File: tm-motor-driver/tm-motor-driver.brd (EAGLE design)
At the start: 68.6 x 19.1 mm, 19 parts

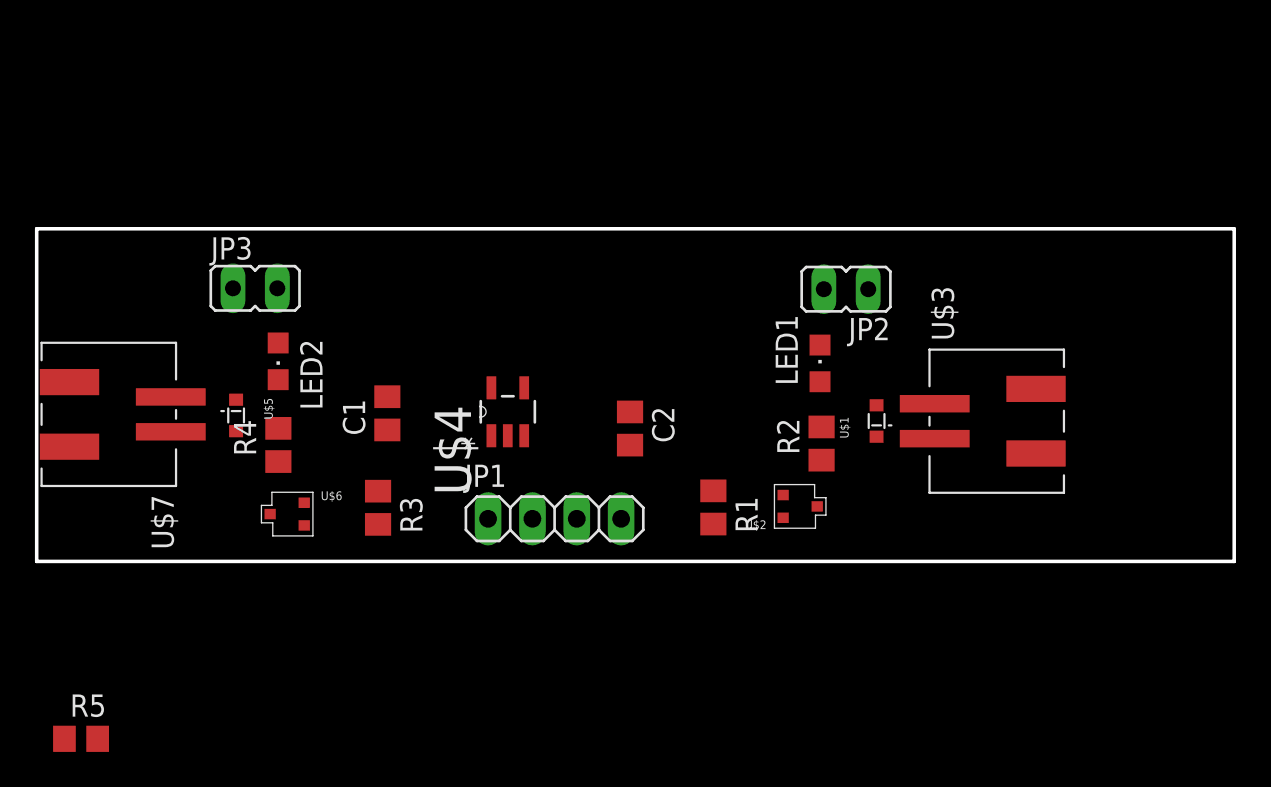
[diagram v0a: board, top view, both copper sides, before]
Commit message: Remove jumpers, rearrange LED and series resistor for easier layout
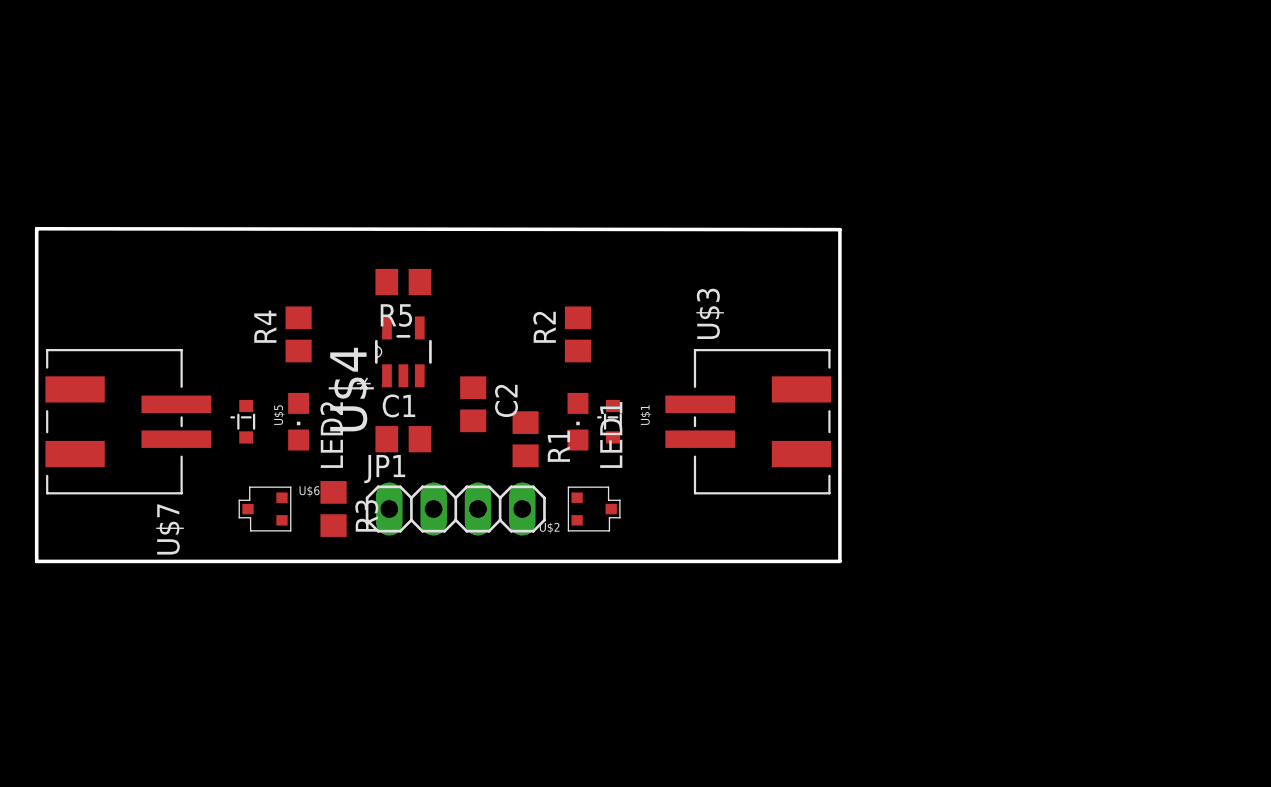
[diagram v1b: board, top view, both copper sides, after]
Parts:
- removed JP2, JP3: (no value), jumper:JP1
- moved R5 32.0 mm to (21.0, 16.0), turned to 180 degrees
- moved R2 15.3 mm to (31.0, 13.0)
- moved U$1 15.1 mm to (33.0, 8.00), turned to 180 degrees
- moved LED1 14.3 mm to (31.0, 8.00), turned to 180 degrees
- moved U$3 13.4 mm to (40.0, 8.00)
- moved U$2 11.8 mm to (32.0, 3.00)
- moved R1 11.4 mm to (28.0, 7.00)
- moved C2 9.09 mm to (25.0, 9.00)
- moved U$4 6.89 mm to (21.0, 12.0)
- moved R4 6.44 mm to (15.0, 13.0)
- moved JP1 5.69 mm to (24.0, 3.00)
- moved LED2 3.65 mm to (15.0, 8.00)
- moved R3 2.55 mm to (17.0, 3.00)
- moved C1 1.74 mm to (21.0, 7.00), turned to 0 degrees
- moved U$6 1.30 mm to (13.0, 3.00)
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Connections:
- removed net N$5: JP3.2, LED2.A
- removed net N$6: LED2.C, R4.2
- net +3V3: now also R2.2, R4.2; no longer JP2.1, JP3.1
- net N$1: now also LED2.C; no longer R4.1
- net N$2: now also LED1.C; no longer R2.1
- net N$3: now also R2.1; no longer JP2.2
- net N$4: now also LED2.A, R4.1; no longer LED1.C, R2.2
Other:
- board size 68.6 x 19.1 mm -> 46 x 19.1 mm

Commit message: Change header to JST
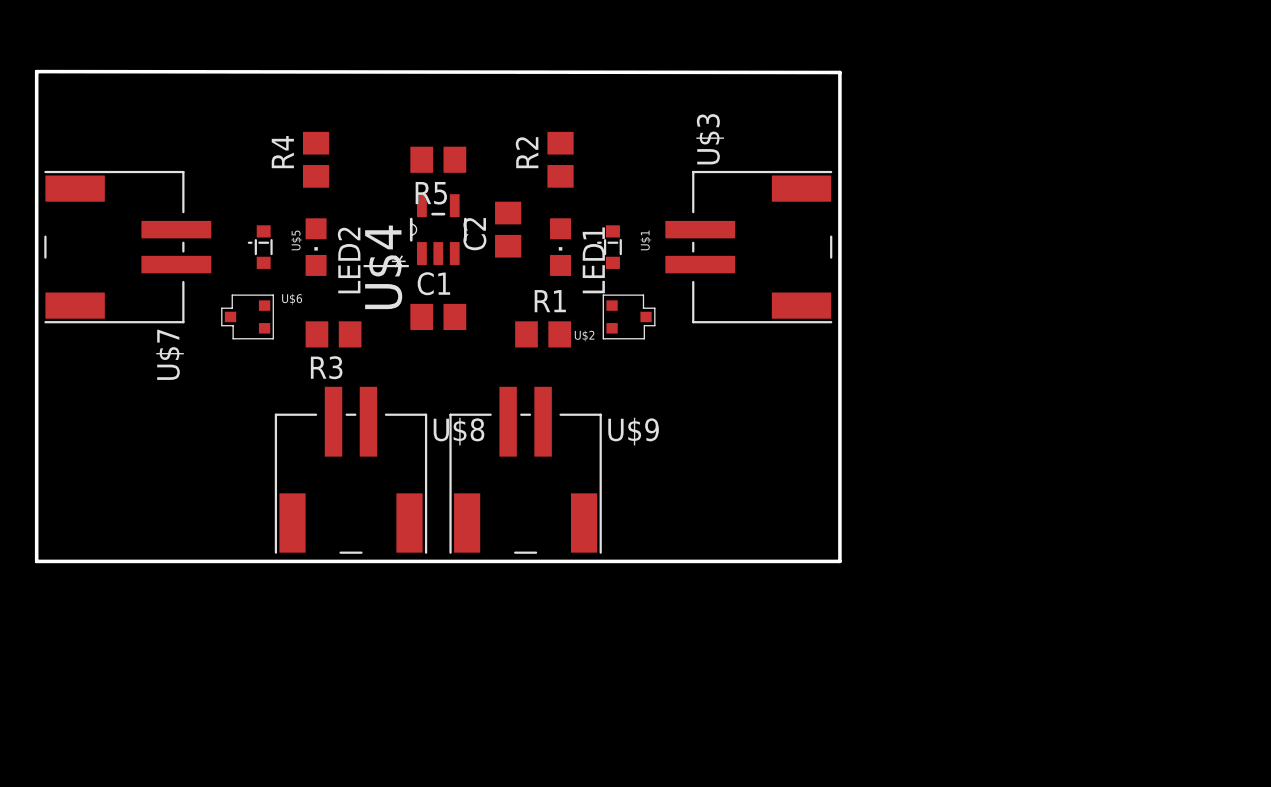
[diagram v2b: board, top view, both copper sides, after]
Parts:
- removed JP1: (no value), pinhead:1X04
- added U$8, U$9: JST-SMD-2, tactile-music:JST-SMD-2
- moved U$2 11.2 mm to (34.0, 14.0)
- moved U$6 11.0 mm to (12.0, 14.0)
- moved C2 10.2 mm to (27.0, 19.0), turned to 90 degrees
- moved LED1 10.0 mm to (30.0, 18.0)
- moved LED2 10.0 mm to (16.0, 18.0)
- moved R2 10.0 mm to (30.0, 23.0)
- moved R4 10.0 mm to (16.0, 23.0)
- moved U$5 10.0 mm to (13.0, 18.0)
- moved R3 10.0 mm to (17.0, 13.0), turned to 180 degrees
- moved U$1 10.0 mm to (33.0, 18.0)
- moved U$3 10.0 mm to (40.0, 18.0)
- moved U$7 10.0 mm to (6.00, 18.0)
- moved C1 7.28 mm to (23.0, 14.0)
- moved R5 7.28 mm to (23.0, 23.0)
- moved U$4 7.28 mm to (23.0, 19.0)
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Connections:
- net BATT_V+: now also U$8.2; no longer JP1.4
- net GND: now also U$8.1; no longer JP1.3
- net PWM0: now also U$9.2; no longer JP1.2
- net PWM1: now also U$9.1; no longer JP1.1
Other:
- board size 46 x 19.1 mm -> 46 x 28.1 mm

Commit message: Change MOTOR_0 JST connections to make PCB routing easier
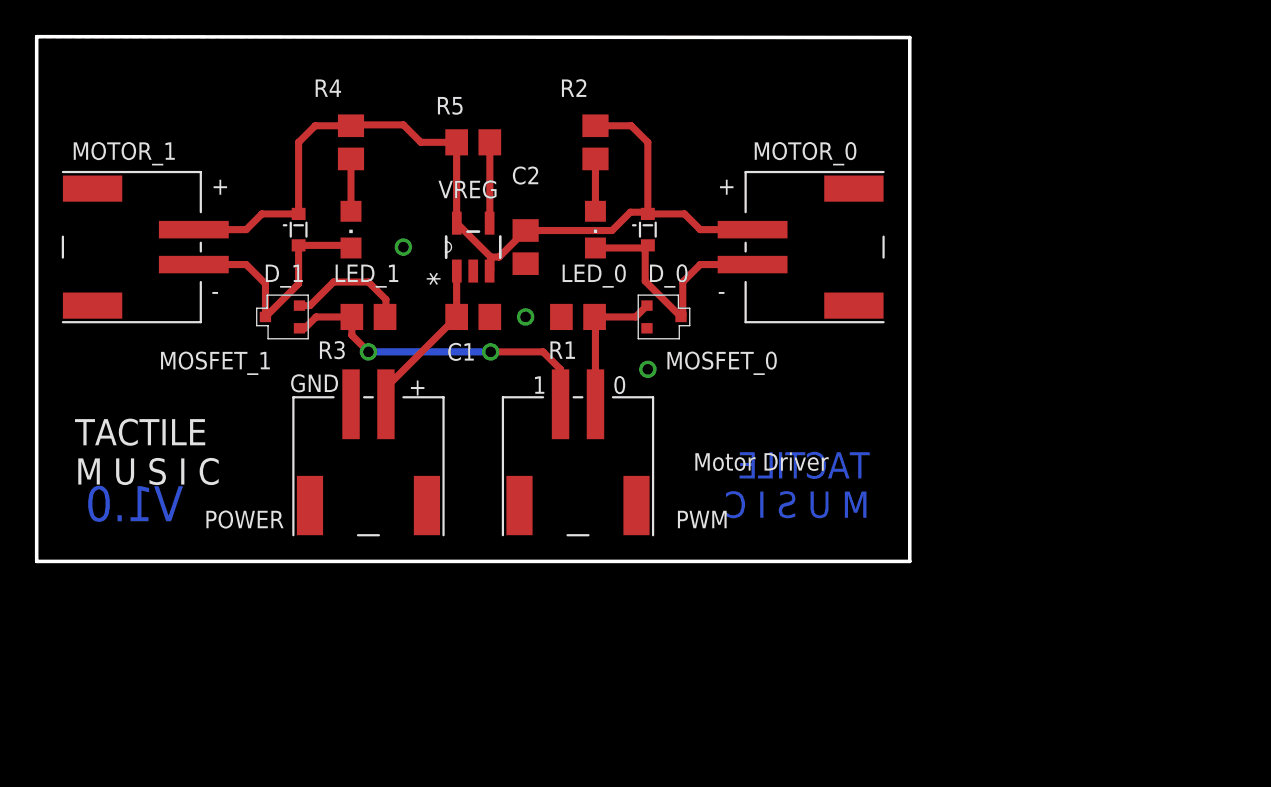
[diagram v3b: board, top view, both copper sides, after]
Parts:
- removed LED1, LED2: (no value), led:CHIPLED_0805
- removed U$1, U$5: DB2S308, tactile-music:SOD-523
- removed U$2, U$6: PMF370XN, tactile-music:SOT323(SC-70)
- removed U$3, U$7, U$8, U$9: JST-SMD-2, tactile-music:JST-SMD-2
- removed U$4: MCP1824T-3302E/OT, tactile-music:SOT95P270X145-5N
- added D_0, D_1: DB2S308, tactile-music:SOD-523
- added LED_0, LED_1: (no value), led:CHIPLED_0805
- added MOSFET_0, MOSFET_1: PMF370XN, tactile-music:SOT323(SC-70)
- added MOTOR_0, MOTOR_1, POWER, PWM: JST-SMD-2, tactile-music:JST-SMD-2
- added VREG: MCP1824T-3302E/OT, tactile-music:SOT95P270X145-5N
- moved R1 2.24 mm to (31.0, 14.0)
- moved R2 2.24 mm to (32.0, 24.0)
- moved R3 2.24 mm to (19.0, 14.0)
- moved R4 2.24 mm to (18.0, 24.0)
- moved R5 2.24 mm to (25.0, 24.0)
- moved C1 2.00 mm to (25.0, 14.0)
- moved C2 1.41 mm to (28.0, 18.0), turned to 270 degrees
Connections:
- net +3V3: now also D_0.1, D_1.1, MOTOR_0.2, MOTOR_1.1, VREG.3, VREG.5; no longer U$1.1, U$3.1, U$4.3, U$4.5, U$5.1, U$7.1
- net BATT_V+: now also POWER.2, VREG.1; no longer U$4.1, U$8.2
- net GND: now also MOSFET_0.2, MOSFET_1.2, POWER.1, VREG.2; no longer U$2.2, U$4.2, U$6.2, U$8.1
- net N$1: now also D_1.2, LED_1.C, MOSFET_1.3, MOTOR_1.2; no longer LED2.C, U$5.2, U$6.3, U$7.2
- net N$2: now also D_0.2, LED_0.C, MOSFET_0.3, MOTOR_0.1; no longer LED1.C, U$1.2, U$2.3, U$3.2
- net N$3: now also LED_0.A; no longer LED1.A
- net N$4: now also LED_1.A; no longer LED2.A
- net N$7: now also VREG.4; no longer U$4.4
- net PWM0: now also MOSFET_0.1, PWM.2; no longer U$2.1, U$9.2
- net PWM1: now also MOSFET_1.1, PWM.1; no longer U$6.1, U$9.1
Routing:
- net +3V3: track 0.00 -> 53.0 mm
- net PWM1: track 0.00 -> 19.1 mm, vias 0 -> 2
- net N$1: track 0.00 -> 14.4 mm
- net N$2: track 0.00 -> 14.3 mm
- net BATT_V+: track 0.00 -> 9.32 mm
- net PWM0: track 0.00 -> 8.29 mm
- net GND: track 0.00 -> 6.94 mm, vias 0 -> 3
- net N$7: track 0.00 -> 4.64 mm
- net N$4: track 0.00 -> 3.00 mm
- net N$3: track 0.00 -> 3.00 mm
- added copper zone on layer 1, net GND
- added copper zone on layer 16, net GND
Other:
- board size 46 x 28.1 mm -> 50 x 30.1 mm
- board text added: "+"
- board text added: "-"
- board text added: "0"
- board text added: "1"
- board text added: "GND"
- board text added: "Motor Driver"
- board text added: "TACTILE M U S I C"
- board text added: "V1.0"

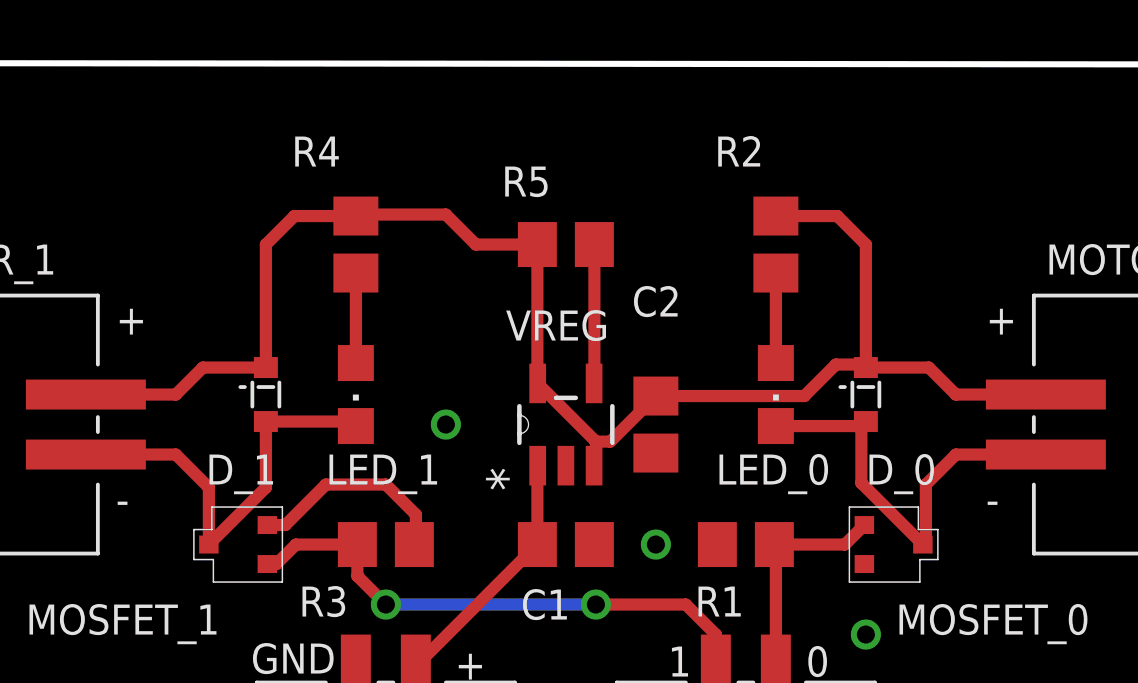
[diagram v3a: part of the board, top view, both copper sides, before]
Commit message: Fixed simple schematic errors, and made some PCB fixes / enhancements
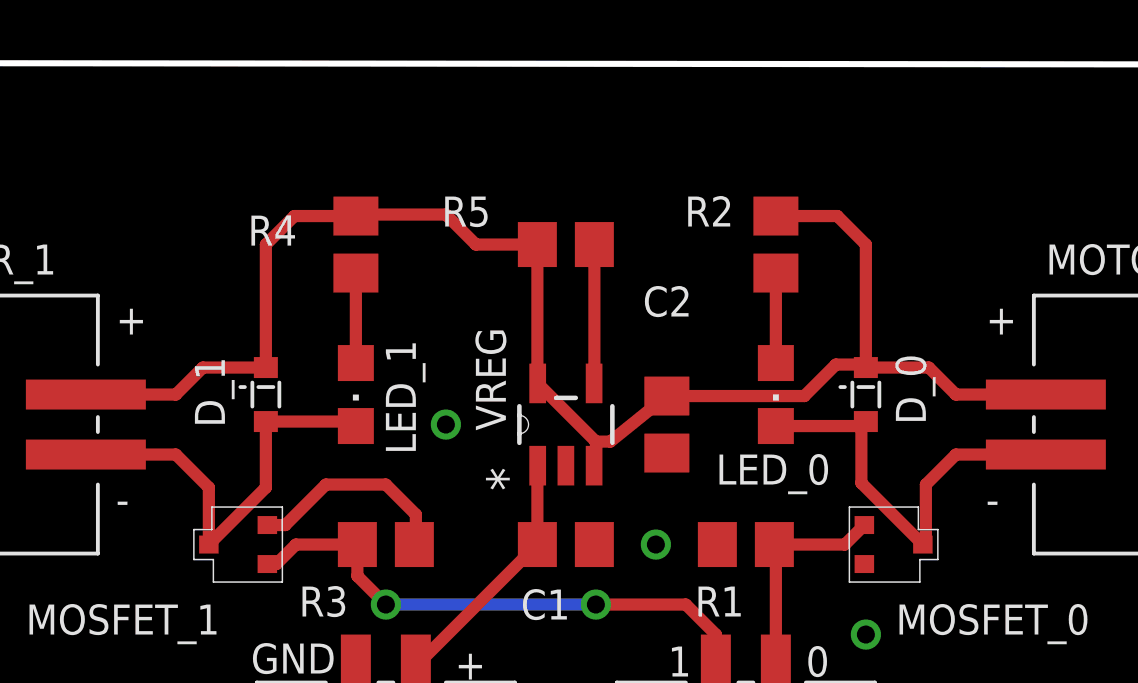
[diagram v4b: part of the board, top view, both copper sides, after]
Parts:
- LED_0, LED_1: value (none) -> RED
- moved C2 0.36 mm to (28.4, 18.0)
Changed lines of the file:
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@@
 <attribute name="VALUE" x="23.6" y="10" size="1" layer="27" font="vector" ratio="20"/>
 </element>
-<element name="C2" library="rcl" package="C0805" value="10uF" x="28" y="18" smashed="yes" rot="R270">
-<attribute name="NAME" x="27.2" y="21.6" size="1" layer="25" font="vector" ratio="20"/>
-<attribute name="VALUE" x="27.2" y="20.4" size="1" layer="27" font="vector" ratio="20"/>
+<element name="C2" library="rcl" package="C0805" value="10uF" x="28.365" y="18" smashed="yes" rot="R270">
+<attribute name="NAME" x="27.565" y="21.6" size="1" layer="25" font="vector" ratio="20"/>
+<attribute name="VALUE" x="27.565" y="20.4" size="1" layer="27" font="vector" ratio="20"/>
 </element>
-<element name="LED_0" library="led" package="CHIPLED_0805" value="" x="32" y="19" smashed="yes" rot="R180">
+<element name="LED_0" library="led" package="CHIPLED_0805" value="RED" x="32" y="19" smashed="yes" rot="R180">
 <attribute name="NAME" x="30" y="16" size="1" layer="25" font="vector" ratio="20"/>
-<attribute name="VALUE" x="29.46" y="20.27" size="1.27" layer="27" rot="R270"/>
 </element>
-<element name="LED_1" library="led" package="CHIPLED_0805" value="" x="18" y="19" smashed="yes" rot="R180">
-<attribute name="NAME" x="17" y="16" size="1" layer="25" font="vector" ratio="20"/>
-<attribute name="VALUE" x="15.46" y="20.27" size="1.27" layer="27" rot="R270"/>
+<element name="LED_1" library="led" package="CHIPLED_0805" value="RED" x="18" y="19" smashed="yes" rot="R180">
+<attribute name="NAME" x="20" y="17" size="1" layer="25" font="vector" ratio="20" rot="R90"/>
 </element>
 <element name="R1" library="resistor" package="R0805" value="10k" x="31" y="14" smashed="yes">
@@
 </element>
 <element name="R2" library="resistor" package="R0805" value="60" x="32" y="24" smashed="yes" rot="R90">
-<attribute name="NAME" x="31.6" y="27.6" size="1" layer="25" font="vector" ratio="20" rot="R180"/>
-<attribute name="VALUE" x="34.2" y="27.5" size="1" layer="27" font="vector" ratio="20" rot="R180"/>
+<attribute name="NAME" x="30.6" y="25.6" size="1" layer="25" font="vector" ratio="20" rot="R180"/>
+<attribute name="VALUE" x="30.39" y="24.325" size="1" layer="27" font="vector" ratio="20" rot="R180"/>
 </element>
 <element name="R3" library="resistor" package="R0805" value="10k" x="19" y="14" smashed="yes" rot="R180">
@@
 </element>
 <element name="R4" library="resistor" package="R0805" value="60" x="18" y="24" smashed="yes" rot="R90">
-<attribute name="NAME" x="17.5" y="27.6" size="1" layer="25" font="vector" ratio="20" rot="R180"/>
-<attribute name="VALUE" x="20.1" y="27.5" size="1" layer="27" font="vector" ratio="20" rot="R180"/>
+<attribute name="NAME" x="16.04" y="24.965" size="1" layer="25" font="vector" ratio="20" rot="R180"/>
+<attribute name="VALUE" x="16.1" y="23.5" size="1" layer="27" font="vector" ratio="20" rot="R180"/>
 </element>
 <element name="D_0" library="tactile-music" package="SOD-523" value="DB2S308" x="35" y="19" smashed="yes" rot="R180">
-<attribute name="NAME" x="35" y="16" size="1" layer="25" font="vector" ratio="20"/>
+<attribute name="NAME" x="37" y="18" size="1" layer="25" font="vector" ratio="20" rot="R90"/>
 </element>
 <element name="MOSFET_0" library="tactile-music" package="SOT323(SC-70)" value="PMF370XN" x="36" y="14" smashed="yes" rot="R180">
@@
 <attribute name="OC_NEWARK" value="40M0704" x="25" y="18" size="1.778" layer="27" rot="R90" display="off"/>
 <attribute name="MPN" value="MCP1824T-3302E/OT" x="25" y="18" size="1.778" layer="27" rot="R90" display="off"/>
-<attribute name="NAME" x="23" y="20.8" size="1" layer="25" font="vector" ratio="20" rot="SR0"/>
+<attribute name="NAME" x="23" y="17.8" size="1" layer="25" font="vector" ratio="20" rot="SR90"/>
 </element>
 <element name="D_1" library="tactile-music" package="SOD-523" value="DB2S308" x="15" y="19" smashed="yes" rot="R180">
-<attribute name="NAME" x="13" y="16" size="1" layer="25" font="vector" ratio="20"/>
+<attribute name="NAME" x="13.635" y="17.905" size="1" layer="25" font="vector" ratio="20" rot="R90"/>
 </element>
 <element name="MOSFET_1" library="tactile-music" package="SOT323(SC-70)" value="PMF370XN" x="14" y="14" smashed="yes">
@@
 </element>
 <element name="R5" library="resistor" package="R0805" value="10k" x="25" y="24" smashed="yes" rot="R180">
-<attribute name="NAME" x="24.5" y="26.6" size="1" layer="25" font="vector" ratio="20" rot="R180"/>
-<attribute name="VALUE" x="27.9" y="26.6" size="1" layer="27" font="vector" ratio="20" rot="R180"/>
+<attribute name="NAME" x="22.5" y="25.6" size="1" layer="25" font="vector" ratio="20" rot="R180"/>
+<attribute name="VALUE" x="22.82" y="24.06" size="1" layer="27" font="vector" ratio="20" rot="R180"/>
 </element>
 <element name="POWER" library="tactile-music" package="JST-SMD-2" value="JST-SMD-2" x="19" y="7" smashed="yes">
@@
 <wire x1="38" y1="19" x2="41" y2="19" width="0.4064" layer="1"/>
 <wire x1="26" y1="17.4318" x2="26.4818" y2="17.4318" width="0.4064" layer="1"/>
-<wire x1="26.4818" y1="17.4318" x2="28" y2="18.95" width="0.4064" layer="1"/>
-<wire x1="28" y1="18.95" x2="32.95" y2="18.95" width="0.4064" layer="1"/>
+<wire x1="26.4818" y1="17.4318" x2="28.365" y2="18.95" width="0.4064" layer="1"/>
+<wire x1="28.365" y1="18.95" x2="32.95" y2="18.95" width="0.4064" layer="1"/>
 <wire x1="32.95" y1="18.95" x2="34" y2="20" width="0.4064" layer="1"/>
 <wire x1="34" y1="20" x2="34.9" y2="20" width="0.4064" layer="1"/>
